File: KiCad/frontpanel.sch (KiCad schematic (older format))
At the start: 26 parts, among them P1 CONN_02X13, P2 CONN_02X13

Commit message: Flipped the pinpads on the frontpanel board ...
... so that we don't have to twist the cables.
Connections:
- net at AFF1.10 (E3): now also P2.5 (P5); no longer P2.6 (P6)
- net at AFF1.11 (D3): now also P2.7 (P7); no longer P2.8 (P8)
- net at AFF1.12 (C3): now also P2.9 (P9); no longer P2.10 (P10)
- net at AFF1.14 (E4): now also P2.19 (P19); no longer P2.20 (P20)
- net at AFF1.15 (D4): now also P2.21 (P21); no longer P2.22 (P22)
- net at AFF1.16 (G4): now also P2.15 (P15); no longer P2.16 (P16)
- net at AFF1.17 (C4): now also P2.23 (P23); no longer P2.24 (P24)
- net at AFF1.19 (B4): now also P2.25 (P25); no longer P2.26 (P26)
- net at AFF1.20 (A4): now also P2.26 (P26); no longer P2.25 (P25)
- net at AFF1.21 (F4): now also P2.17 (P17); no longer P2.18 (P18)
- net at AFF1.24 (B3): now also P2.11 (P11); no longer P2.12 (P12)
- net at AFF1.25 (A3): now also P2.13 (P13); no longer P2.14 (P14)
- net at AFF1.26 (G3): now also P2.1 (P1); no longer P2.2 (P2)
- net at AFF1.27 (F3): now also P2.3 (P3); no longer P2.4 (P4)
- net at AFF1.28 (B2): now also P2.12 (P12); no longer P2.11 (P11)
- net at AFF1.29 (A2): now also P2.14 (P14); no longer P2.13 (P13)
- net at AFF1.30 (F2): now also P2.4 (P4); no longer P2.3 (P3)
- net at AFF1.5 (E2): now also P2.6 (P6); no longer P2.5 (P5)
- net at AFF1.6 (D2): now also P2.8 (P8); no longer P2.7 (P7)
- net at AFF1.7 (G2): now also P2.2 (P2); no longer P2.1 (P1)
- net at AFF1.8 (C2): now also P2.10 (P10); no longer P2.9 (P9)
- net at AFF1.9 (DP2): now also P2.16 (P16); no longer P2.15 (P15)
- net at JSW1.0: now also P1.12 (P12)
- net at P1.11 (P11): now also LD1.3 (A2); no longer JSW1.0
- net at JSW2.0: now also P1.14 (P14)
- net at P1.13 (P13): now also LD1.1 (A1); no longer JSW2.0
- net at P1.10 (P10): now also MSW4.0; no longer MD1.1 (K)
- net at P1.15 (P15): now also LD2.3 (A2); no longer JSW3.0
- net at P1.16 (P16): now also JSW3.0; no longer LD2.3 (A2)
- net at P1.17 (P17): now also LD2.1 (A1); no longer JSW4.0
- net at P1.18 (P18): now also JSW4.0; no longer LD2.1 (A1)
- net at P1.19 (P19): now also LD3.3 (A2); no longer RSW1.0
- net at P1.20 (P20): now also RSW1.0; no longer LD3.3 (A2)
- net at P1.21 (P21): now also LD3.1 (A1); no longer PSW1.0
- net at P1.22 (P22): now also PSW1.0; no longer LD3.1 (A1)
- net at P1.23 (P23): now also LD4.3 (A2); no longer CSW1.0
- net at P1.24 (P24): now also CSW1.0; no longer LD4.3 (A2)
- net at LD1.2 (K), LD2.2 (K), LD3.2 (K)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: now also P1.26 (P26); no longer P1.25 (P25)
- net at LD4.1 (A1): now also P1.25 (P25); no longer P1.26 (P26)
- net at P1.3 (P3): now also MD4.1 (K); no longer MSW1.0
- net at P1.4 (P4): now also MSW1.0; no longer MD4.1 (K)
- net at P1.5 (P5): now also MD3.1 (K); no longer MSW2.0
- net at P1.6 (P6): now also MSW2.0; no longer MD3.1 (K)
- net at P1.7 (P7): now also MD2.1 (K); no longer MSW3.0
- net at P1.8 (P8): now also MSW3.0; no longer MD2.1 (K)
- net at P1.9 (P9): now also MD1.1 (K); no longer MSW4.0
- net at RD5.2 (A): now also P2.18 (P18); no longer P2.17 (P17)
- net at PD1.2 (A): now also P2.20 (P20); no longer P2.19 (P19)
- net at SD1.2 (A): now also P2.22 (P22); no longer P2.21 (P21)
- net at SD2.2 (A): now also P2.24 (P24); no longer P2.23 (P23)
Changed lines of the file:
@@
 F 3 "" H 3400 3000 50  0000 C CNN
 	1    3400 4150
-	1    0    0    -1
+	-1   0    0    -1
 $EndComp
 $Comp
@@
 F 3 "" H 9350 2800 50  0000 C CNN
 	1    9350 3950
-	1    0    0    -1
+	-1   0    0    -1
 $EndComp
 $Comp

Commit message: added some metainfo
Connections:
- net at JSW1.0: now also P1.12 (P12)
- net at JSW2.0: now also P1.14 (P14)
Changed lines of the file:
@@
 encoding utf-8
 Sheet 1 1
-Title ""
+Title "Podregilo frontpanel board"
 Date ""
 Rev ""
-Comp ""
+Comp "https://github.com/johannes-mueller/Podregilo"
 Comment1 ""
 Comment2 ""

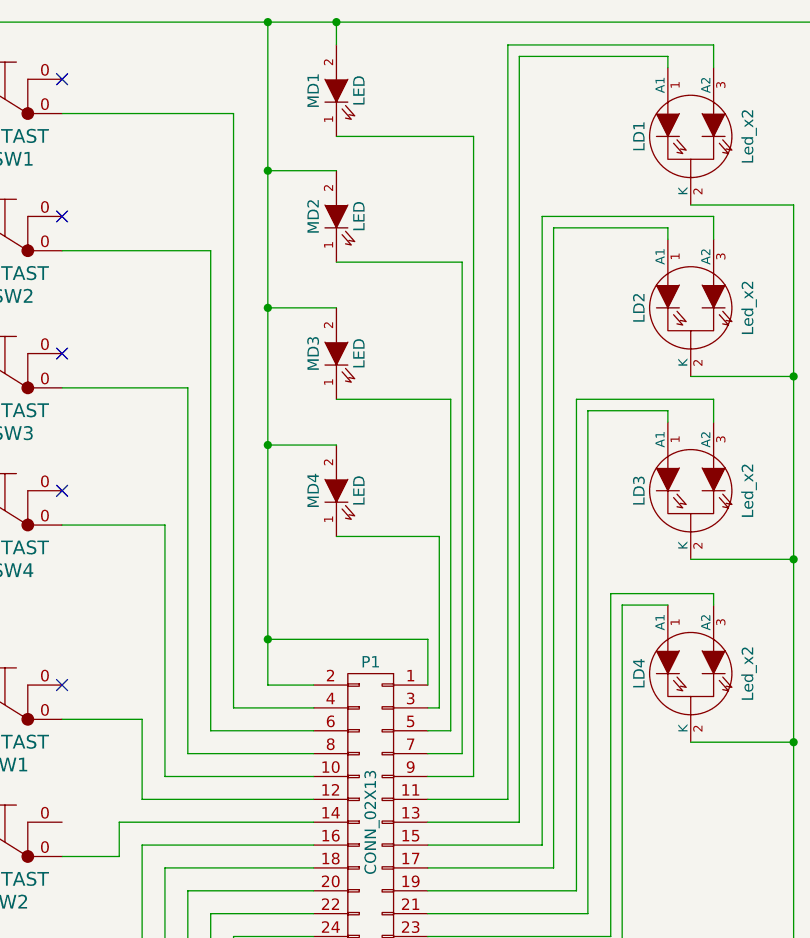
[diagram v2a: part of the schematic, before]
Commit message: fixed wrong led order
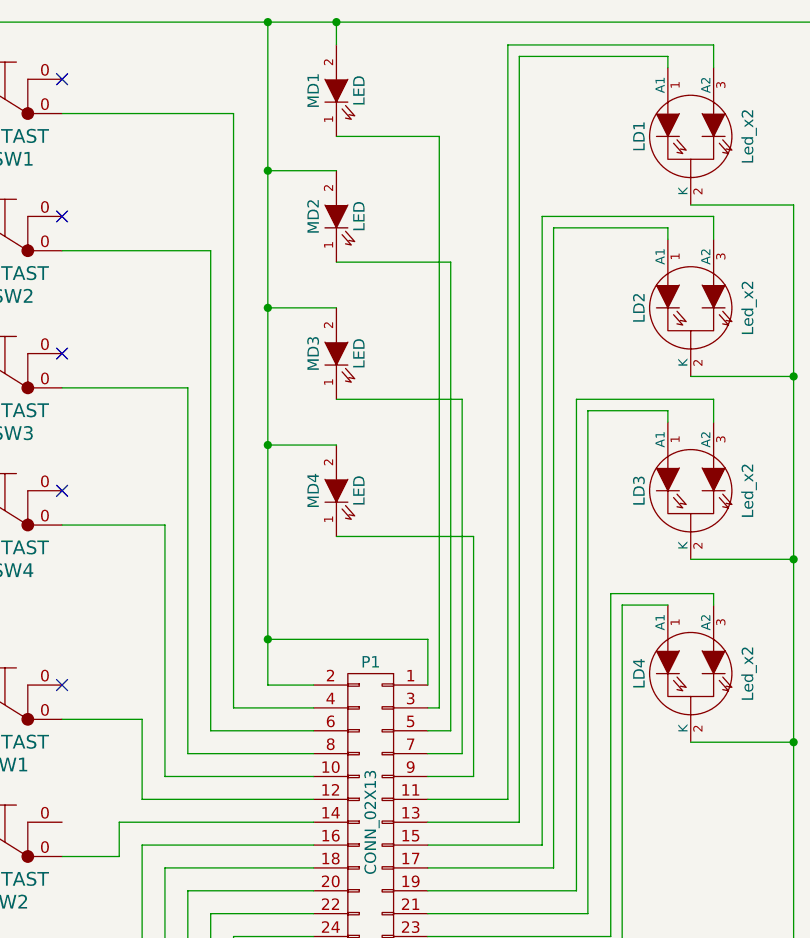
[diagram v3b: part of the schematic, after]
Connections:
- net at JSW1.0: now also P1.12 (P12)
- net at JSW2.0: now also P1.14 (P14)
- net at P1.3 (P3): now also MD1.1 (K); no longer MD4.1 (K)
- net at P1.5 (P5): now also MD2.1 (K); no longer MD3.1 (K)
- net at P1.7 (P7): now also MD3.1 (K); no longer MD2.1 (K)
- net at P1.9 (P9): now also MD4.1 (K); no longer MD1.1 (K)
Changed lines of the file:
@@
 	3650 3550 3650 3350
-Wire Wire Line
-	3250 2900 3700 2900
-Wire Wire Line
-	3700 2900 3700 3650
-Wire Wire Line
-	3700 3650 3650 3650
-Wire Wire Line
-	3250 2300 3750 2300
-Wire Wire Line
-	3750 2300 3750 3750
-Wire Wire Line
-	3750 3750 3650 3750
-Wire Wire Line
-	3250 1700 3800 1700
-Wire Wire Line
-	3800 1700 3800 3850
-Wire Wire Line
-	3800 3850 3650 3850
-Wire Wire Line
-	3250 1150 3850 1150
-Wire Wire Line
-	3850 1150 3850 3950
-Wire Wire Line
-	3850 3950 3650 3950
 Wire Wire Line
 	2950 650  2950 3550
@@
 NoConn ~ 10850 2150
 NoConn ~ 8450 750
+Wire Wire Line
+	3650 3650 3700 3650
+Wire Wire Line
+	3700 3650 3700 1150
+Wire Wire Line
+	3700 1150 3250 1150
+Wire Wire Line
+	3650 3750 3750 3750
+Wire Wire Line
+	3750 3750 3750 1700
+Wire Wire Line
+	3750 1700 3250 1700
+Wire Wire Line
+	3650 3850 3800 3850
+Wire Wire Line
+	3800 3850 3800 2300
+Wire Wire Line
+	3800 2300 3250 2300
+Wire Wire Line
+	3850 3950 3850 2900
+Wire Wire Line
+	3850 2900 3250 2900
+Wire Wire Line
+	3650 3950 3850 3950
 $EndSCHEMATC
